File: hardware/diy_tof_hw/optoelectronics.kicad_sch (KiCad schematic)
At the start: 27 parts, among them IC21 74LVC1G08QW5-7, IC22 LMG1025QDEETQ1, SW1 SW_Nidec_CAS-120A1, U2 OPA858xDSG, U3 TLV3501AIDBV

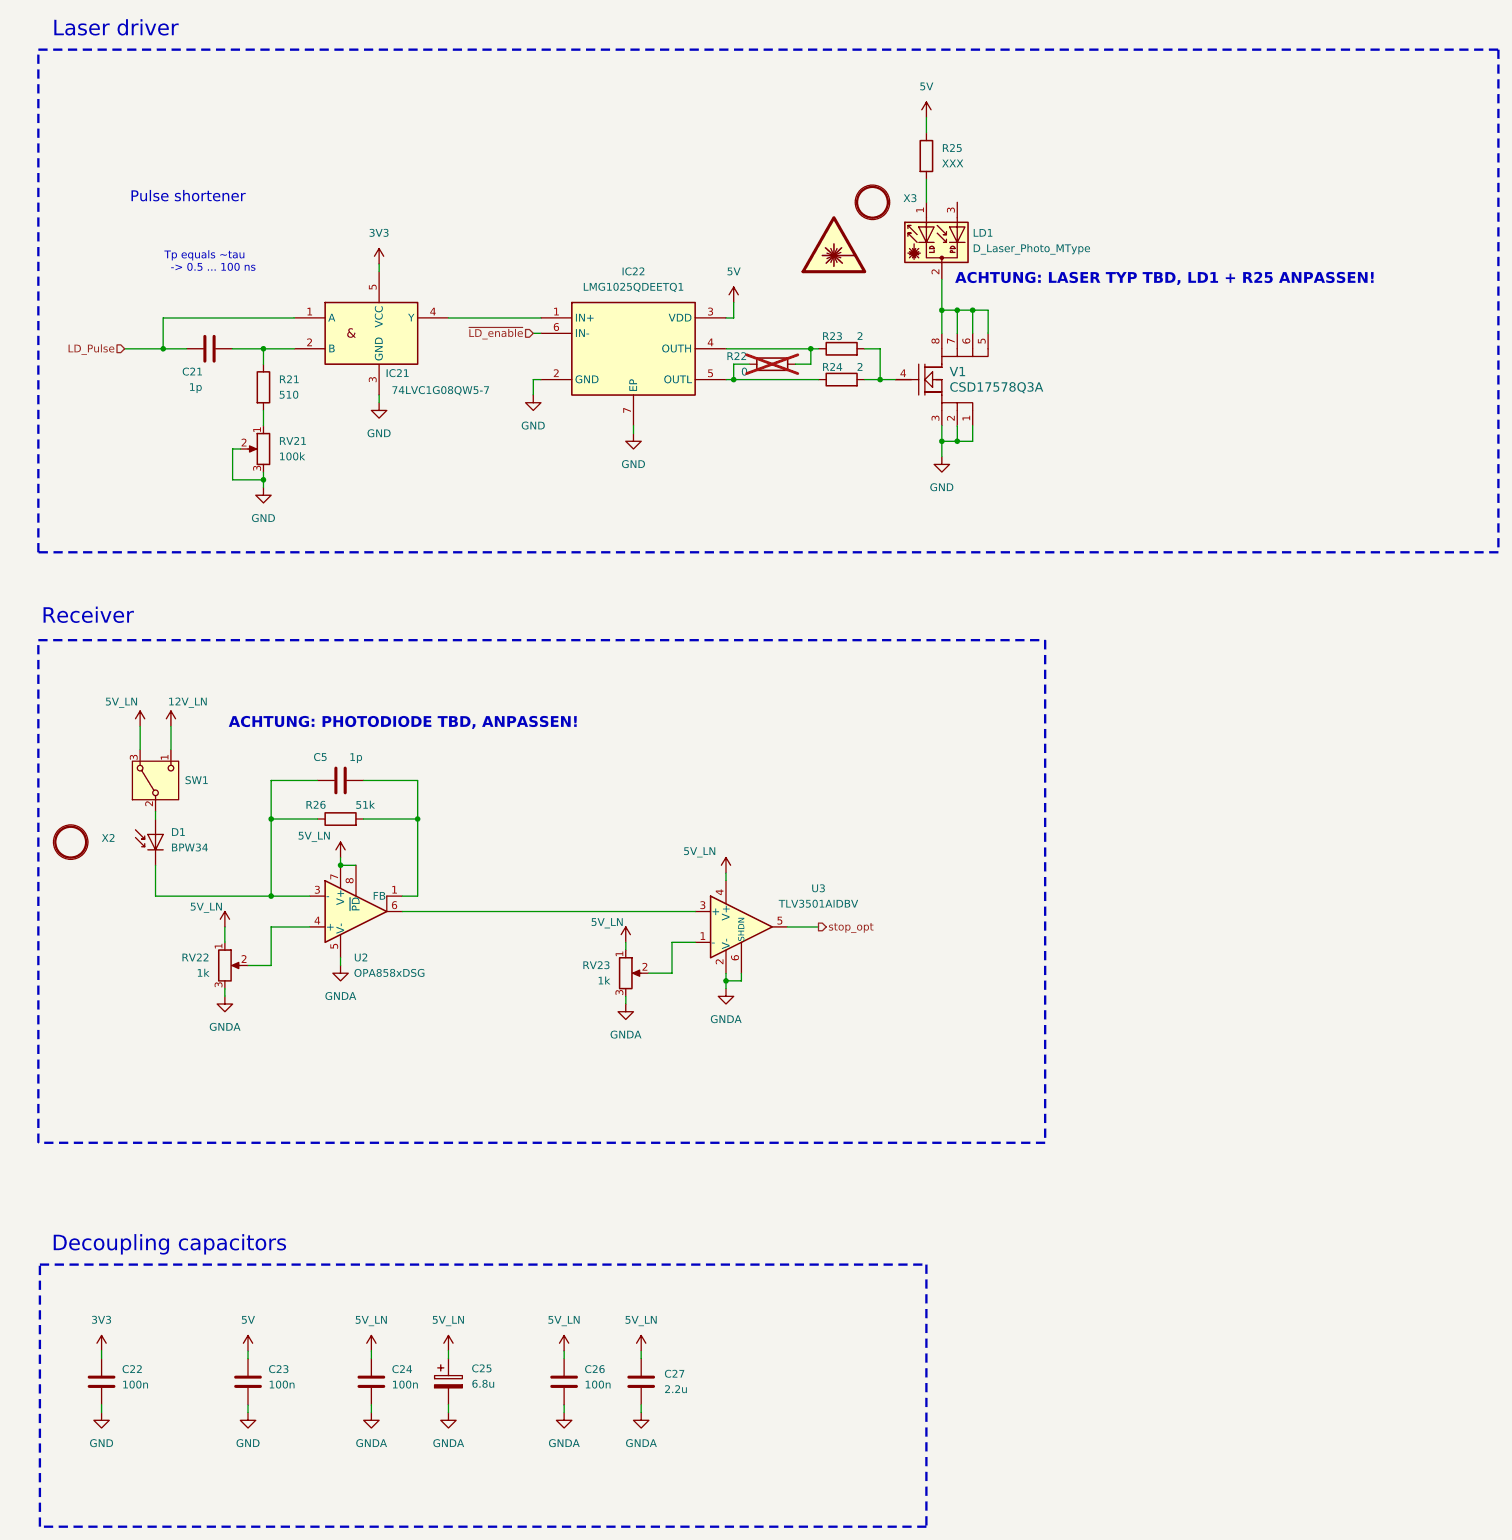
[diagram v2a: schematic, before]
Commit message: [hardware, firmware] various review findings  - added new signals TDC_opt/ele_enable  - fixed placement and appearance of the optics mount  - added switch for stop signal of the electrical TDC  - replaced "ground bead" with a 0R (in order to have a single clamping point for GND)  - added some additional decoupling caps for the laser driver  - reversed polarisation of the PD  - added a small resistor in between TIA and comparator  - adjusted RC to have higher capacitance and lower resistance  - cleaned up some labels / port names
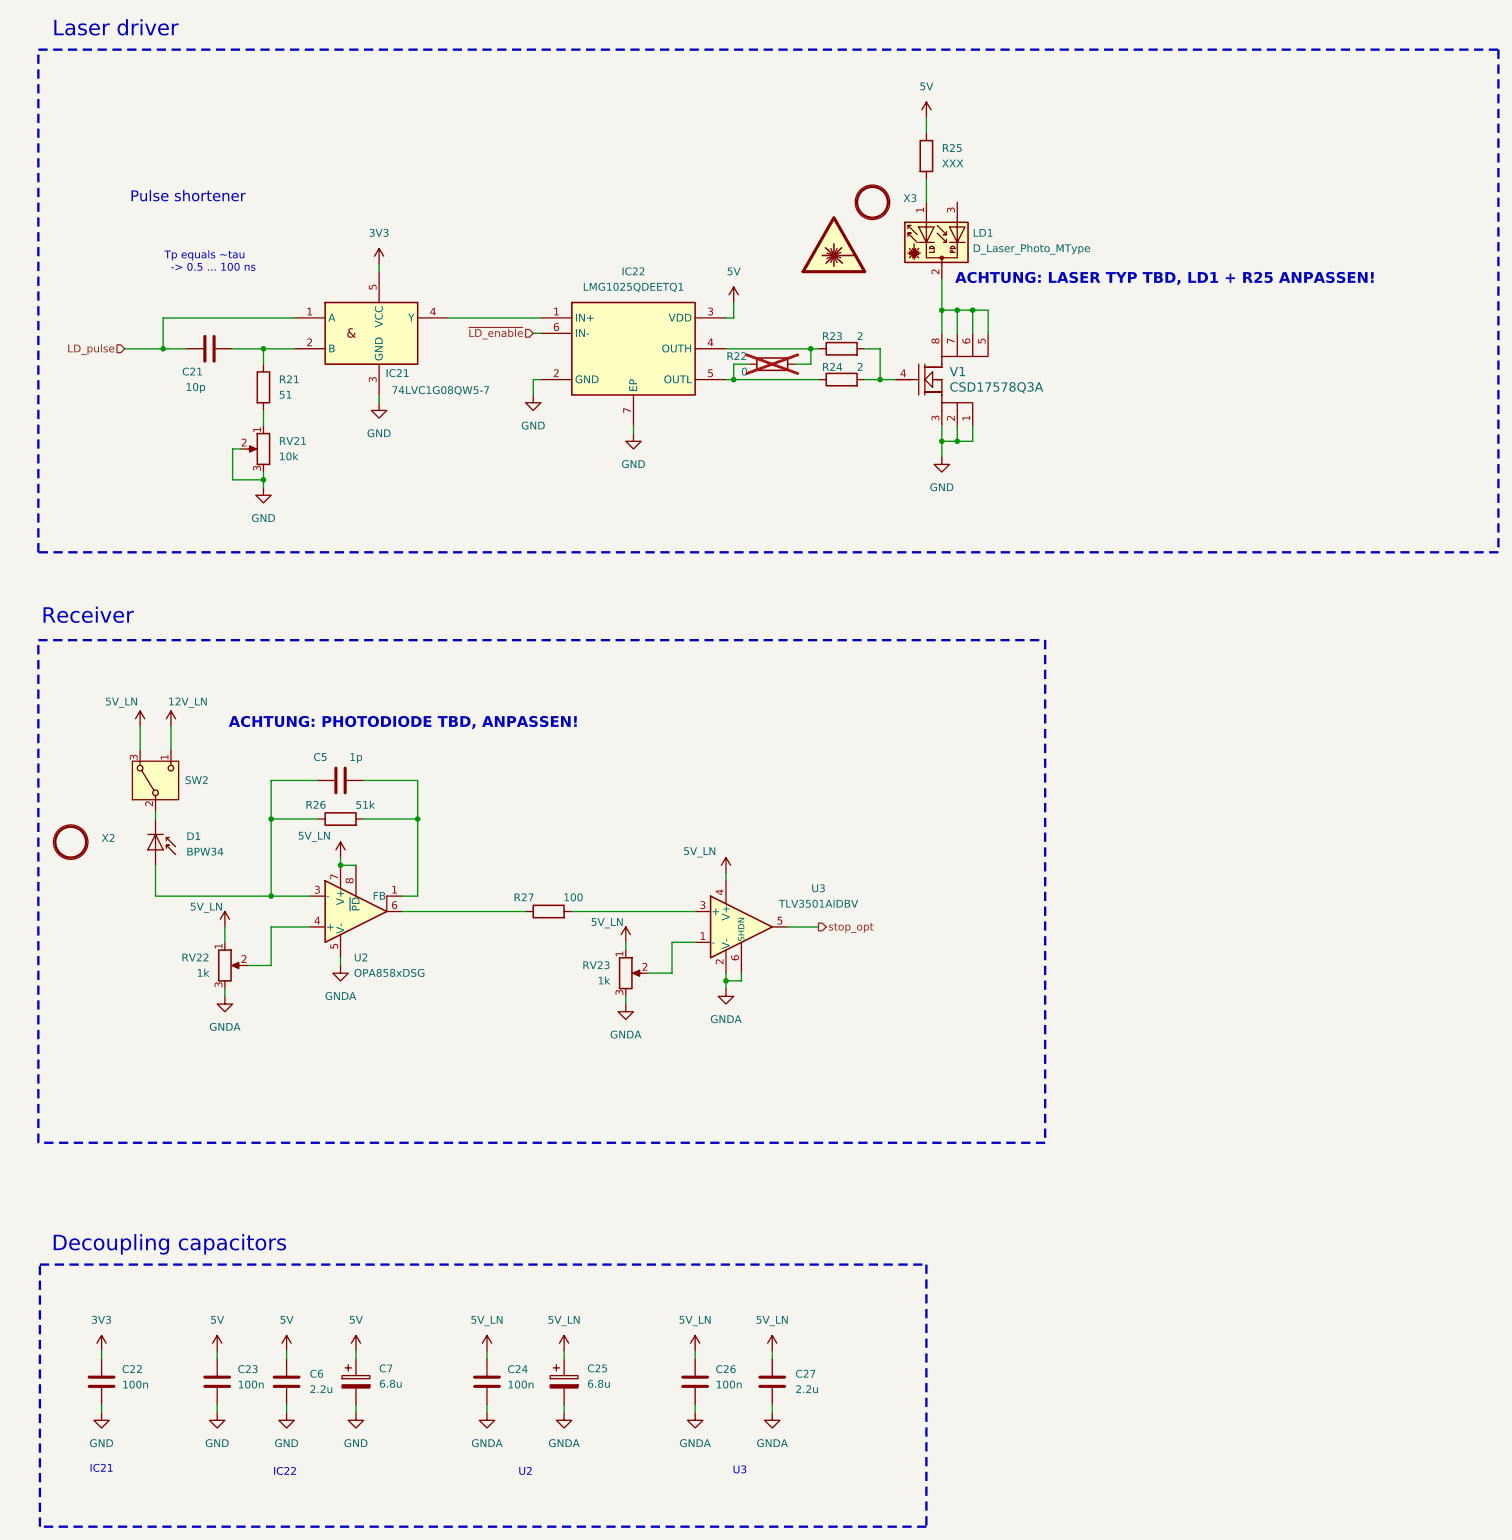
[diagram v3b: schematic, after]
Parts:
- added C6: 2.2u, Capacitor_SMD:C_0603_1608Metric_Pad1.08x0.95mm_HandSolder, symbol Device:C
- added C7: 6.8u, Capacitor_Tantalum_SMD:CP_EIA-7343-43_Kemet-X_Pad2.25x2.55mm_HandSolder, symbol Device:C_Polarized
- added R27: 100, Resistor_SMD:R_0402_1005Metric_Pad0.72x0.64mm_HandSolder, symbol Device:R
- C21: value 1p -> 10p
- R21: value 510 -> 51
- RV21: value 100k -> 10k
- renumbered SW1 to SW2
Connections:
- net 5V: now also C6.1, C7.1
- net GND: now also C6.2, C7.2
- net at C5.1, R26.1, U2.3 (-): now also D1.2 (A); no longer D1.1 (K)
- net at SW2.2 (B): now also D1.1 (K); no longer D1.2 (A)
- net at U3.3 (+): now also R27.2; no longer U2.6
- net LD_Pulse renamed LD_pulse
- new net: R27.1, U2.6
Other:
- note added: "IC21"
- note added: "IC22"
- note added: "U2"
- note added: "U3"
- moved on the sheet: C23, C24, C25, C26, C27

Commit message: [hardware] added various testpoints, some minor other fixes on the layout (designators)
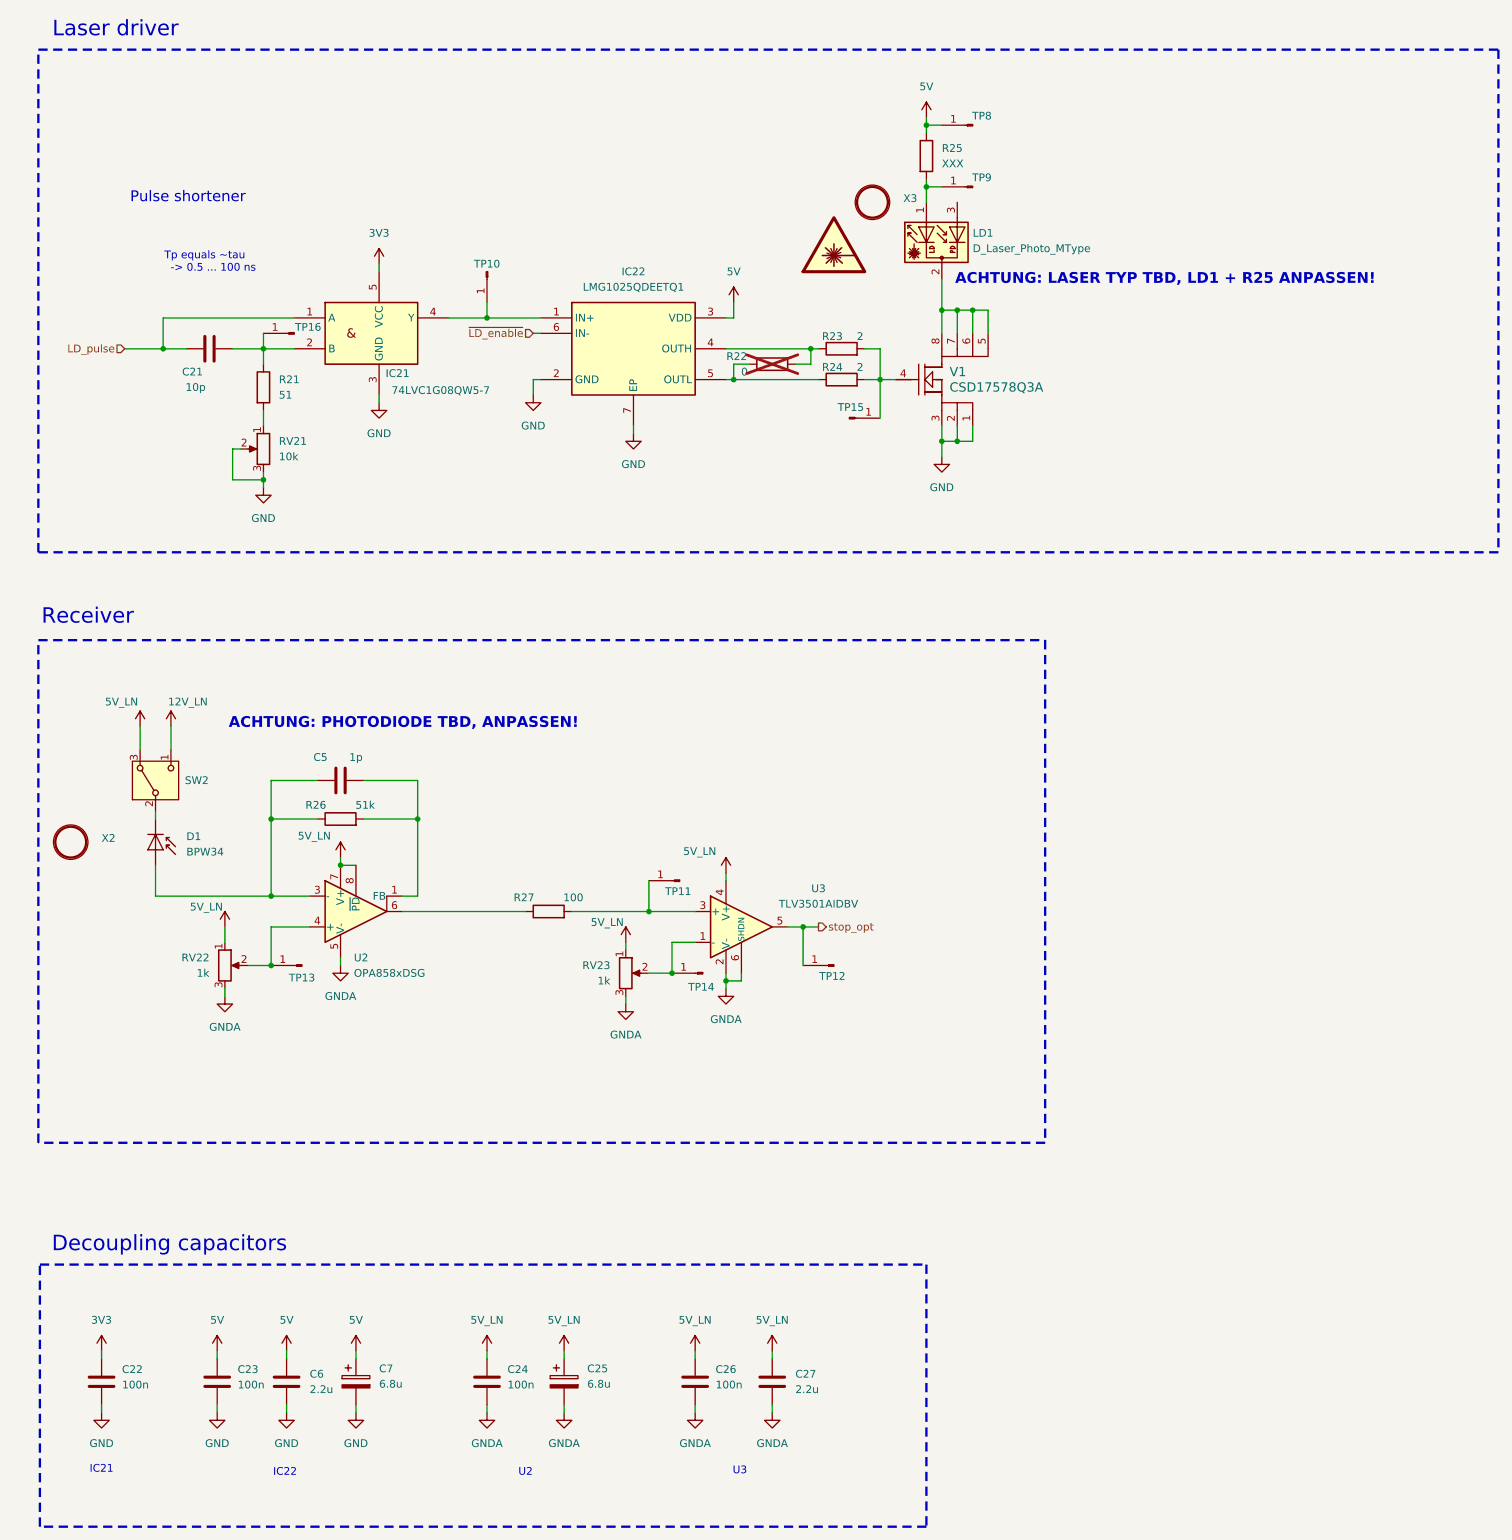
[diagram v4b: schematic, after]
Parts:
- added TP10, TP11, TP12, TP13, TP14, TP15, TP16, TP8, TP9: Conn_01x01_Pin, Connector_PinHeader_2.54mm:PinHeader_1x01_P2.54mm_Vertical, symbol Connector:Conn_01x01_Pin
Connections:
- net 5V: now also TP8.1 (Pin_1)
- net stop_opt: now also TP12.1 (Pin_1)
- net at R23.2, R24.2, V1.4: now also TP15.1 (Pin_1)
- net at IC21.4 (Y), IC22.1 (IN+): now also TP10.1 (Pin_1)
- net at LD1.1, R25.2: now also TP9.1 (Pin_1)
- net at RV22.2, U2.4 (+): now also TP13.1 (Pin_1)
- net at RV23.2, U3.1 (-): now also TP14.1 (Pin_1)
- net at R27.2, U3.3 (+): now also TP11.1 (Pin_1)
- net at C21.2, IC21.2 (B), R21.1: now also TP16.1 (Pin_1)
